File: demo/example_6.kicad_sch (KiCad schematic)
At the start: 23 parts, among them U6 AP3032

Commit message: Update demo project for upcoming changes
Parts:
- R21: KiVar.Rule I_LED_MA 80,90,100,110,120,130,140,150(+!) JP() -> (none); Var (none) -> I_LED_MA 80,90,100,110,120,130,140,150(+!) JP()
- R22: KiVar.Rule I_LED_MA 40,50,60,70,120,130,140,150(+!) JP() -> (none); Var (none) -> I_LED_MA 40,50,60,70,120,130,140,150(+!) JP()
- R29: KiVar.Rule I_LED_MA 20,30,60,70,100,110,140,150(+!) JP() -> (none); Var (none) -> I_LED_MA 20,30,60,70,100,110,140,150(+!) JP()
- R30: KiVar.Rule I_LED_MA 10,30,50,70,90,110,130,150(+!) JP() -> (none); Var (none) -> I_LED_MA 10,30,50,70,90,110,130,150(+!) JP()
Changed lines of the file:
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@@
 	(title_block
 		(title "KiVar Demo")
-		(date "2024-03-18")
+		(date "2024-03-19")
 		(rev "0.1.0")
 		(company "Author: Mark Hämmerling <dev@markh.de>")
@@
 			)
 		)
-		(property "KiVar.Rule" "I_LED_MA 20,30,60,70,100,110,140,150(+!) JP()"
+		(property "Var" "I_LED_MA 20,30,60,70,100,110,140,150(+!) JP()"
 			(at 119.38 119.3799 0)
 			(effects
@@
 		(fields_autoplaced yes)
 		(property "Reference" "U6"
-			(at 83.82 51.435 0)
-			(effects
-				(font
-					(size 1.27 1.27)
-				)
-				(justify left)
+			(at 91.44 48.26 0)
+			(effects
+				(font
+					(size 1.27 1.27)
+				)
 			)
 		)
 		(property "Value" "AP3032"
-			(at 99.06 51.435 0)
-			(effects
-				(font
-					(size 1.27 1.27)
-				)
-				(justify right)
+			(at 91.44 50.8 0)
+			(effects
+				(font
+					(size 1.27 1.27)
+				)
 			)
 		)
@@
 			)
 		)
-		(property "KiVar.Rule" "I_LED_MA 80,90,100,110,120,130,140,150(+!) JP()"
+		(property "Var" "I_LED_MA 80,90,100,110,120,130,140,150(+!) JP()"
 			(at 119.38 74.2949 0)
 			(effects
@@
 			)
 		)
-		(property "KiVar.Rule" "I_LED_MA 40,50,60,70,120,130,140,150(+!) JP()"
+		(property "Var" "I_LED_MA 40,50,60,70,120,130,140,150(+!) JP()"
 			(at 187.96 74.2949 0)
 			(effects
@@
 			)
 		)
-		(property "KiVar.Rule" "I_LED_MA 10,30,50,70,90,110,130,150(+!) JP()"
+		(property "Var" "I_LED_MA 10,30,50,70,90,110,130,150(+!) JP()"
 			(at 187.96 119.3799 0)
 			(effects

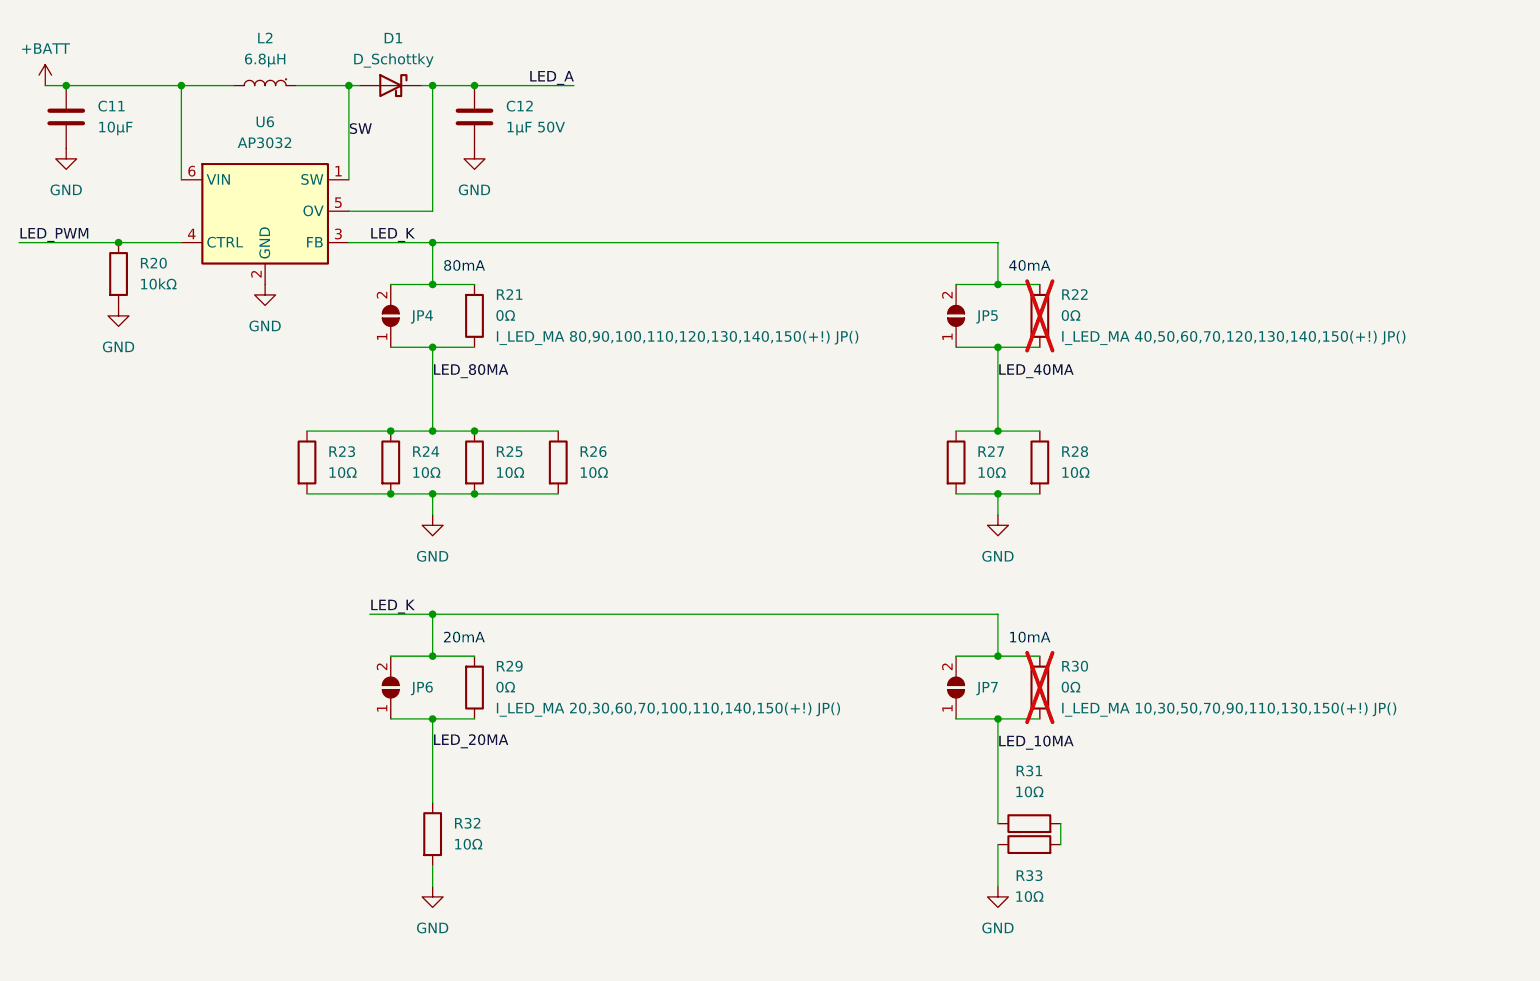
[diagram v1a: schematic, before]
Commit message: Make use of new 0.2.0 features in demo project, use different expression types
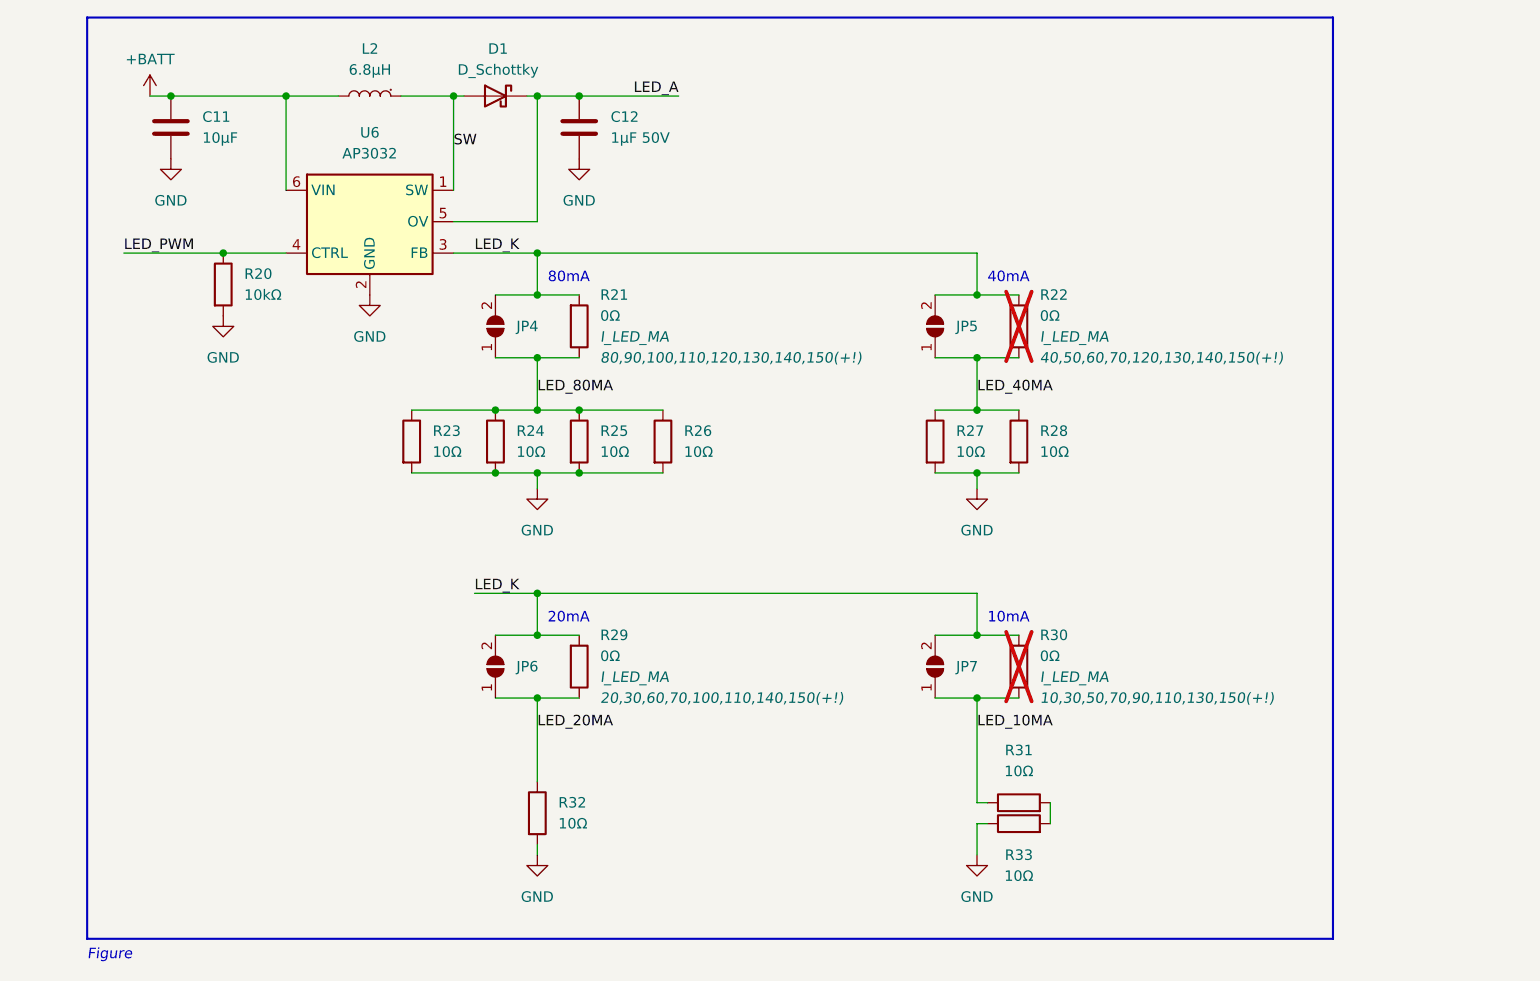
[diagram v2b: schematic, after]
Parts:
- R21: Var I_LED_MA 80,90,100,110,120,130,140,150(+!) JP() -> 80,90,100,110,120,130,140,150(+!); Var.Aspect (none) -> I_LED_MA
- R22: Var I_LED_MA 40,50,60,70,120,130,140,150(+!) JP() -> 40,50,60,70,120,130,140,150(+!); Var.Aspect (none) -> I_LED_MA
- R29: Var I_LED_MA 20,30,60,70,100,110,140,150(+!) JP() -> 20,30,60,70,100,110,140,150(+!); Var.Aspect (none) -> I_LED_MA
- R30: Var I_LED_MA 10,30,50,70,90,110,130,150(+!) JP() -> 10,30,50,70,90,110,130,150(+!); Var.Aspect (none) -> I_LED_MA
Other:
- note added: "Figure"
- moved on the sheet: C11, C12, D1, JP4, JP5, JP6, JP7, L2, R20, R21, R22, R23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
